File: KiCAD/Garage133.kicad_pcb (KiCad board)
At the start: 4 copper layers, 97.8 x 39.4 mm, 56 parts, among them J1 Edge2x6_Connector, J2 USB_B_Micro, K1 SANYOU_SRD_Form_C, K2 SANYOU_SRD_Form_C, Q2 UMH3N, Q3 MMBT3906, Q4 MMBT3906, U1 ESP32-WROOM-32, U2 AMS1117-3.3, U3 SHTC3

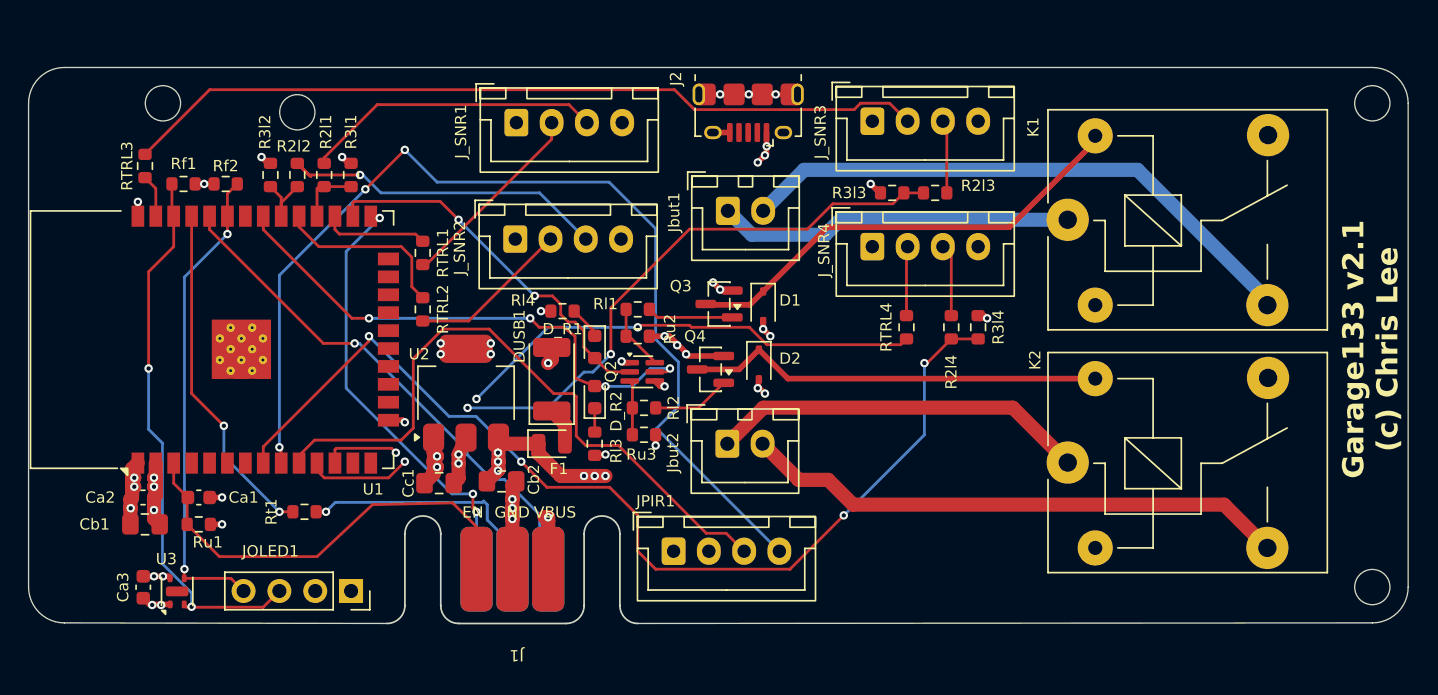
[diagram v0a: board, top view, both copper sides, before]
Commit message: Version 2.1.0: four sonars, USB-C (#26)
## [2.1.0] - 2026-10-14

### Added
- **Hardware Board v3.1 & Enclosure Updates**: KiCAD PCB updates for
board v3.1 with revised BOM, updated 3D printable enclosure (better
SHTC3 thermal isolation, labeled connectors, improved USB-C port
clearance), and solder stencil support frame model.
- **HMM Visualization & Retraining Workflow**: Added
`analysis/hmm_to_svg.py` to generate SVG state transition diagrams from
trained HMM models, and added characterization workflow in
`analysis/retrain.py`.

### Changed
- **Sonar Watchdog & Timeout Stability**: Added sonar ping timeout
handling to prevent blocking pulses from triggering the ESP32 hardware
watchdog.

### Removed
- **Retired Legacy Hardware**: Removed firmware and PlatformIO
configuration support for legacy Classic ESP32 boards (Board v1/v2 /
`node32s`), focusing entirely on Board v3.x (ESP32-S3).

## [2.0.0] - 2026-08-21

### Added
- **Hardware Board v3.0 & ESP32-S3 Support**: Added PlatformIO
configuration (`usb_s3`), pin assignments for ESP32-S3, updated
schematic/PCB designs, and refreshed solder stencil fixture 3D models.
- **Quad-Sonar Support**: Integrated dual ultrasonic sensors per side (4
total) with updated state classification logic, training pipeline, and
retrained HMM models.
- **Home Assistant Probability Export**: Exported garage state
probabilities (`probOpen`, `probCar`, `probEmpty`) via Home Assistant
MQTT discovery.

### Changed
- **Svelte Build Tooling**: Pinned `svelteesp32` to v3.2.5 and updated
CI workflows to Node 22 for reproducible builds.
- **Dependency & Workflow Upgrades**: Upgraded `og3` to v0.6.3,
`og3x-oled` to v0.6.1, and updated GitHub Actions workflows to latest
versions.
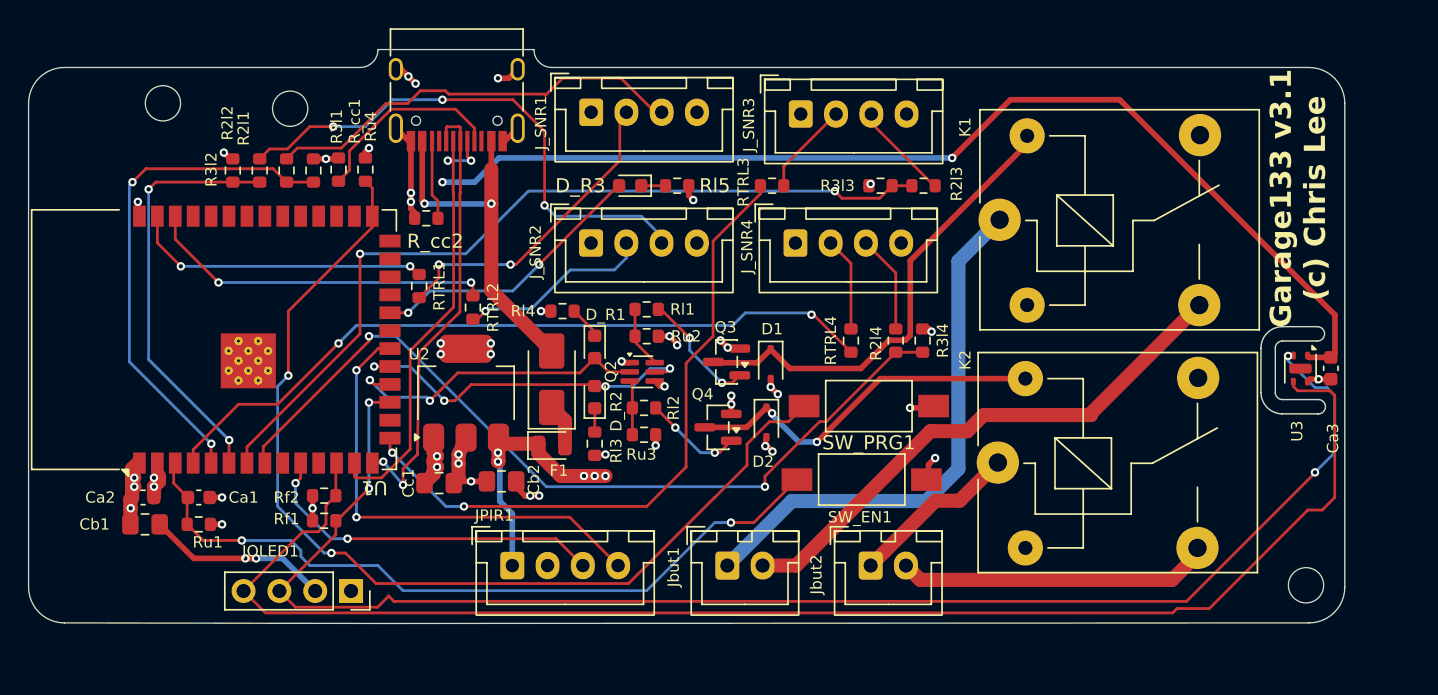
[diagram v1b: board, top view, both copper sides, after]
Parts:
- removed J2: USB_B_Micro, Connector_USB:USB_Micro-B_Amphenol_10118194_Horizontal
- removed the REF** at (80.0, 51.4)
- removed the REF** at (156.2, 50.8)
- removed Rt1: 470, Resistor_SMD:R_0603_1608Metric
- added D_R3: YLW, LED_SMD:LED_0603_1608Metric, F.Cu at (103.6, 56.6)
- added REF**: MountingHole_2.5mm, MountingHole:MountingHole_2.5mm, F.Cu at (79.5, 51.2)
- added R_cc1: 5.1k, Resistor_SMD:R_0603_1608Metric, F.Cu at (82.9, 55.5)
- added R_cc2: 5.1k, Resistor_SMD:R_0603_1608Metric, F.Cu at (89.2, 58.9)
- added Rl5: 1k, Resistor_SMD:R_0603_1608Metric, F.Cu at (106.9, 56.6)
- added Ru4: 10k, Resistor_SMD:R_0603_1608Metric, F.Cu at (84.8, 55.5)
- added SW_EN1: SW_Push, Button_Switch_SMD:SW_SPST_FSMSM, F.Cu at (120.0, 77.5)
- added SW_PRG1: SW_Push, Button_Switch_SMD:SW_SPST_FSMSM, F.Cu at (120.5, 72.3)
- D1, D2: value D -> B5817WS-TP
- DUSB1: footprint Diode_SMD:D_2010_5025Metric -> Diode_SMD:D_SMA
- J1: value Edge2x6_Connector -> USB_C_Receptacle_USB2.0_16P; footprint chl33_library:EdgeConnector_2x3 -> Connector_USB:USB_C_Receptacle_HRO_TYPE-C-31-M-12
- Q3, Q4: value MMBT3906 -> MMBT4403
- U1: value ESP32-WROOM-32 -> ESP32-S3-WROOM-1; footprint RF_Module:ESP32-WROOM-32 -> RF_Module:ESP32-S3-WROOM-1
- moved Ca3 85.6 mm to (153.3, 69.6), turned to -90 degrees
- moved U3 81.2 mm to (151.1, 69.6), turned to -90 degrees
- moved RTRL3 44.5 mm to (113.7, 56.6), turned to 0 degrees
- moved J1 37.2 mm to (91.3, 49.4)
- moved Rf1 25.9 mm to (81.9, 80.4), turned to 180 degrees
- moved Jbut1 25.1 mm to (110.5, 83.6)
- moved Rf2 23.2 mm to (81.9, 78.6)
- moved Jbut2 13.3 mm to (120.7, 83.6)
- moved JPIR1 11.5 mm to (95.2, 83.6)
- moved J_SNR4 5.46 mm to (115.3, 60.7)
- moved J_SNR2 5.38 mm to (100.8, 60.7)
- moved J_SNR1 5.35 mm to (100.8, 51.4)
- moved J_SNR3 5.10 mm to (115.7, 51.6)
- moved K2 4.95 mm to (129.7, 76.3)
- moved K1 4.83 mm to (129.8, 59.1)
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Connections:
- Ca1 pad 2: EN -> Net-(U1-EN)
- Cb1 pad 1: +3.3V -> +5V
- Cb2 pad 1: +5V -> +3.3V
- Ru1 pad 1: EN -> Net-(U1-EN)
- U1 pad 11: ECHO3 -> unconnected-(U1-IO18-Pad11)
- U1 pad 12: TRIG4 -> SDA1
- U1 pad 13: unconnected-(U1-IO14-Pad13) -> USB_D-
- U1 pad 14: unconnected-(U1-IO12-Pad14) -> USB_D+
- U1 pad 15: GND -> TRIG3
- U1 pad 17: unconnected-(U1-SHD/SD2-Pad17) -> SCL1
- U1 pad 18: unconnected-(U1-SWP/SD3-Pad18) -> RELAY_CMD1
- U1 pad 19: unconnected-(U1-SCS/CMD-Pad19) -> RELAY_CMD2
- U1 pad 20: unconnected-(U1-SCK/CLK-Pad20) -> AL
- U1 pad 22: unconnected-(U1-SDI/SD1-Pad22) -> LED1
- U1 pad 25: GPIO0 -> unconnected-(U1-IO48-Pad25)
- U1 pad 26: RELAY_CMD1 -> unconnected-(U1-IO45-Pad26)
- U1 pad 27: TRIG1 -> Net-(U1-IO0)
- U1 pad 28: ECHO1 -> unconnected-(U1-IO35-Pad28)
- U1 pad 29: TRIG2 -> unconnected-(U1-IO36-Pad29)
- U1 pad 3: EN -> Net-(U1-EN)
- U1 pad 30: ECHO2 -> unconnected-(U1-IO37-Pad30)
- U1 pad 31: RELAY_CMD2 -> unconnected-(U1-IO38-Pad31)
- U1 pad 33: SDA1 -> unconnected-(U1-IO40-Pad33)
- U1 pad 34: TXC -> unconnected-(U1-IO41-Pad34)
- U1 pad 35: TX -> unconnected-(U1-IO42-Pad35)
- U1 pad 36: SCL1 -> unconnected-(U1-RXD0-Pad36)
- U1 pad 37: TRIG3 -> unconnected-(U1-TXD0-Pad37)
- U1 pad 38: GND -> TRIG2
- U1 pad 39: GND -> TRIG1
- U1 pad 4: unconnected-(U1-SENSOR_VP-Pad4) -> TRIG4
- U1 pad 5: unconnected-(U1-SENSOR_VN-Pad5) -> ECHO1
- U1 pad 6: unconnected-(U1-IO34-Pad6) -> ECHO2
- U1 pad 7: unconnected-(U1-IO35-Pad7) -> ECHO3
- U1 pad 9: AL -> unconnected-(U1-IO16-Pad9)
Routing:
- net +3.3V: track 12.6 -> 87.8 mm, vias 13 -> 14
- net Net-(U1-IO0): track 0.00 -> 71.7 mm, vias 0 -> 2
- net SDA1: track 34.1 -> 104.6 mm, vias 2 -> 0
- net SCL1: track 39.4 -> 106.7 mm, vias 2 -> 4
- net Net-(U1-EN): track 0.00 -> 53.5 mm, vias 0 -> 2
- net Net-(J_SNR3-Pin_2): track 57.3 -> 6.62 mm
- net TRIG3: track 3.05 -> 46.8 mm, vias 0 -> 2
- net AL: track 73.8 -> 33.4 mm, vias 3 -> 2
- net TXC: track 37.0 -> 0.00 mm, vias 1 -> 0
- net USB_D-: track 0.00 -> 32.4 mm, vias 0 -> 2
- net USB_D+: track 0.00 -> 32.0 mm, vias 0 -> 2
- net ECHO1: track 4.32 -> 36.0 mm, vias 0 -> 2
- net EN: track 31.4 -> 0.00 mm
- net GPIO0: track 31.3 -> 0.00 mm, vias 3 -> 0
- net ECHO2: track 4.98 -> 29.9 mm, vias 0 -> 2
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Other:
- board size 97.8 x 39.4 mm -> 93.3 x 40.7 mm
- board text added: "Garage133 v3.1 (c) Chris Lee"
- board text removed: "EN"
- board text removed: "GPIO"
- board text removed: "Garage133 v2.1 (c) Chris Lee"
- board text removed: "RX"
- board text removed: "TX"
- board text removed: "VBUS"
